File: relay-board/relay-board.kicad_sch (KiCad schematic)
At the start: 7 parts, among them J1 24V Select, J2 RA25P

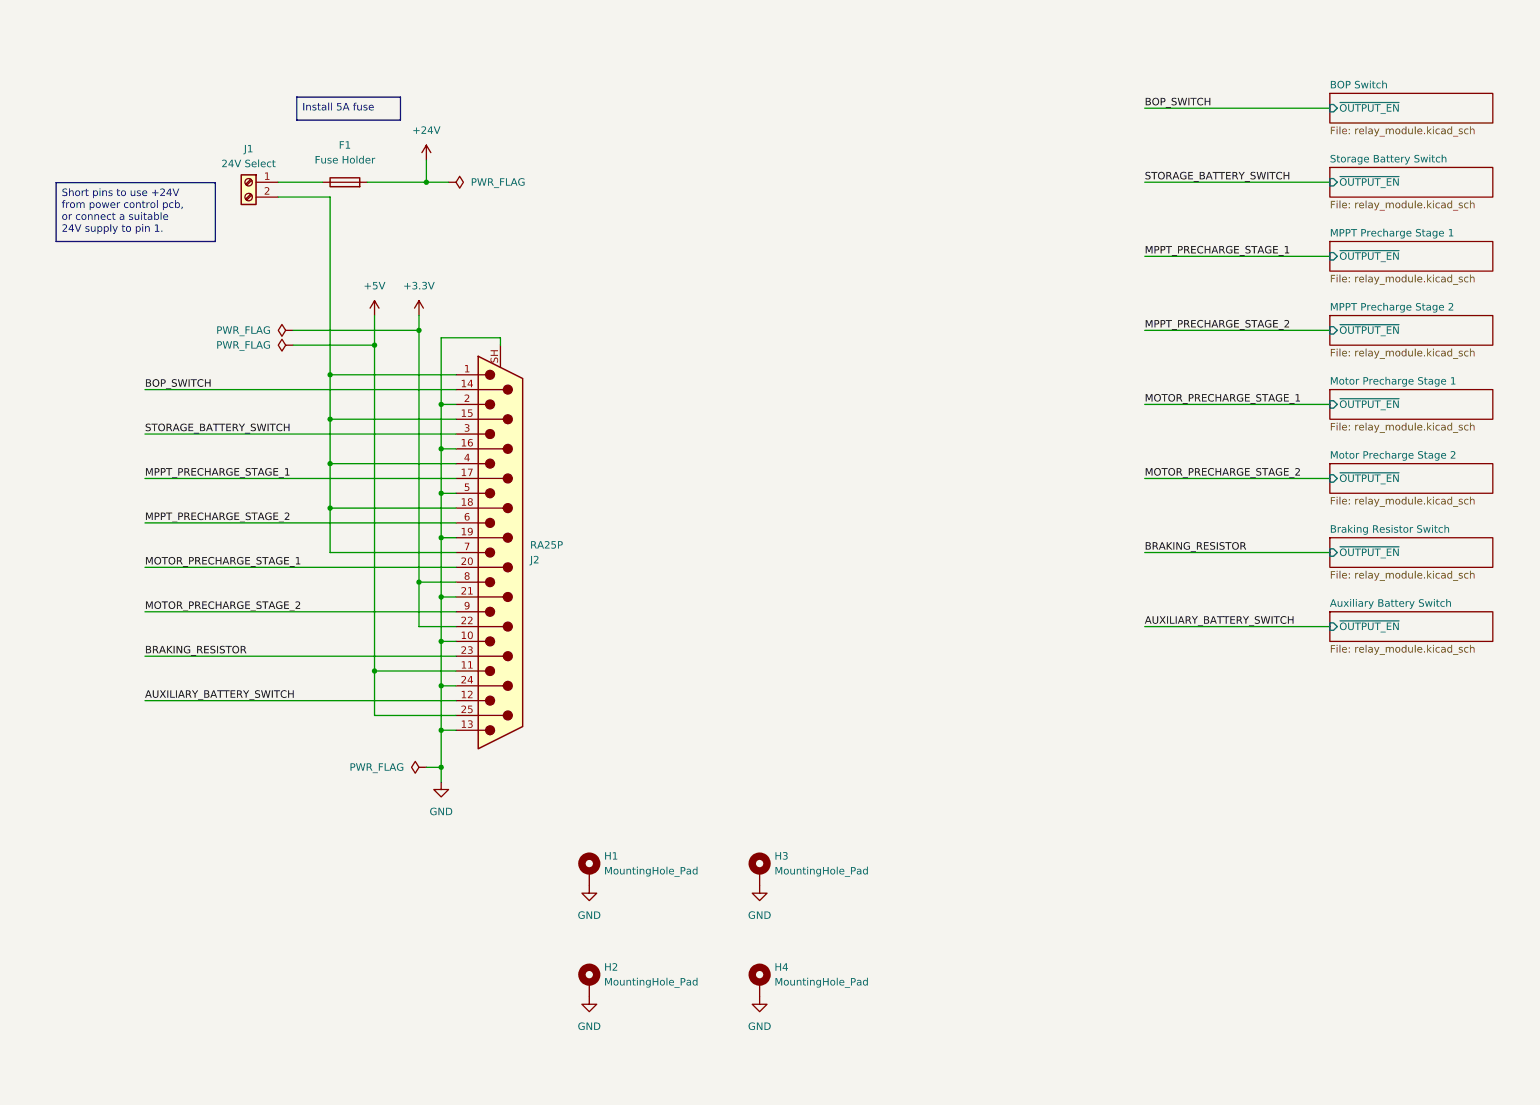
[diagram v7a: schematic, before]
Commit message: relay-board: remove 3.3V input
Reduces risk of shorts and was not necessary to begin with. Now inputs
are active high, which is also less prone to mistakes on the programming
side.
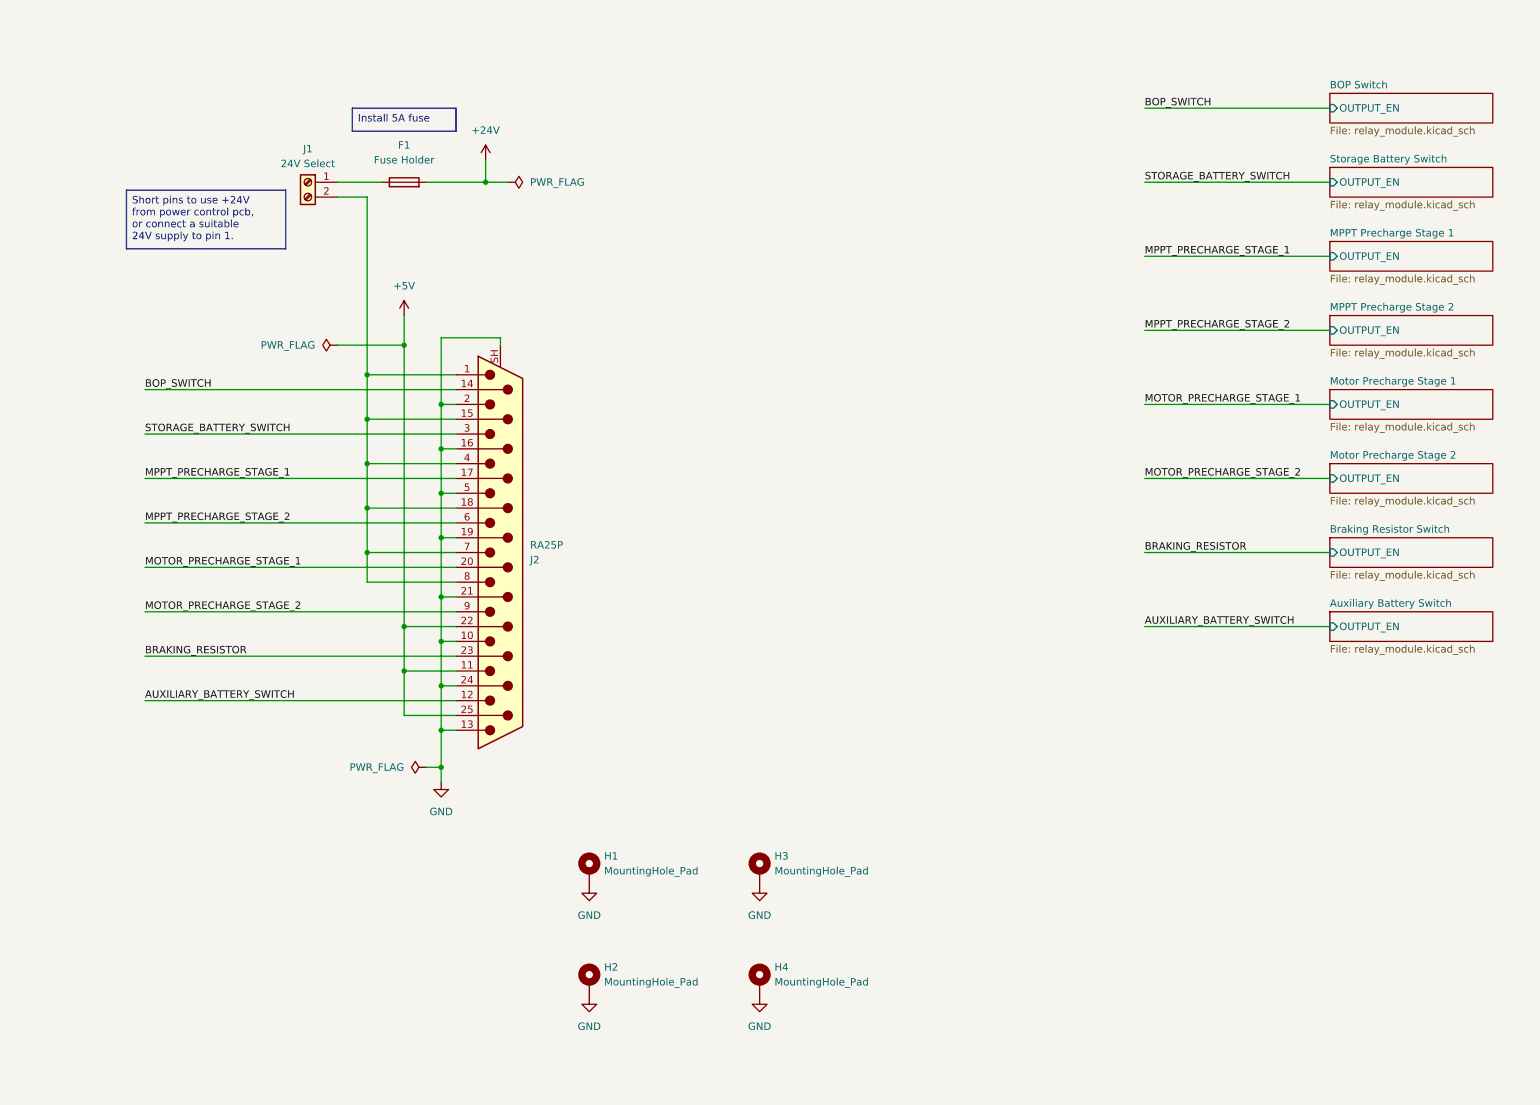
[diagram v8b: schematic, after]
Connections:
- net +5V: now also J2.22 (P22)
- net at J1.2 (Pin_2), J2.1, J2.15 (P15)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: now also J2.8
- removed net +3.3V: J2.22 (P22), J2.8
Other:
- sheet Auxiliary Battery Switch ports: added OUTPUT_EN; removed ~{OUTPUT_EN}
- sheet BOP Switch ports: added OUTPUT_EN; removed ~{OUTPUT_EN}
- sheet Braking Resistor Switch ports: added OUTPUT_EN; removed ~{OUTPUT_EN}
- sheet MPPT Precharge Stage 1 ports: added OUTPUT_EN; removed ~{OUTPUT_EN}
- sheet MPPT Precharge Stage 2 ports: added OUTPUT_EN; removed ~{OUTPUT_EN}
- sheet Motor Precharge Stage 1 ports: added OUTPUT_EN; removed ~{OUTPUT_EN}
- sheet Motor Precharge Stage 2 ports: added OUTPUT_EN; removed ~{OUTPUT_EN}
- sheet Storage Battery Switch ports: added OUTPUT_EN; removed ~{OUTPUT_EN}
- moved on the sheet: F1, J1
